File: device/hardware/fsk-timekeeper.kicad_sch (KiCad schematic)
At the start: 19 parts, among them J1 SENSOR, SW1 SW_SPST, U1 SuperMini nRF52840, U2 Ai-Thinker Ra-01SH, U3 TPS61040DBV

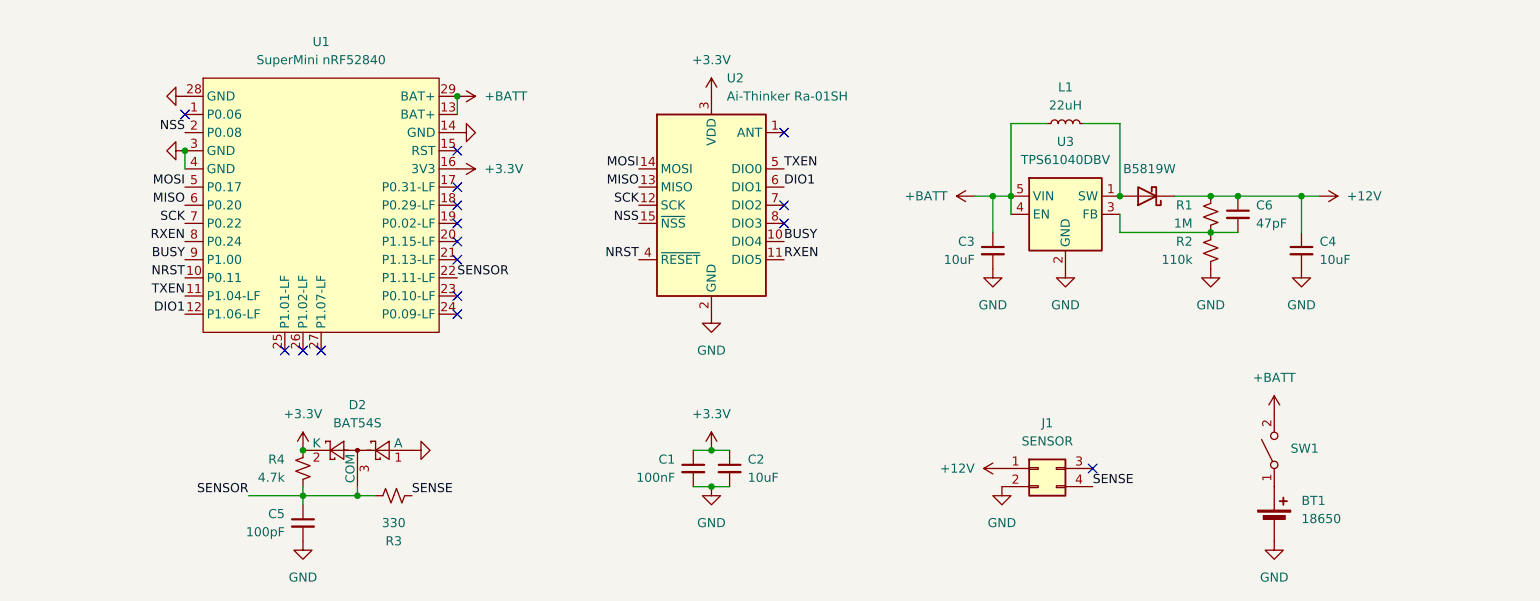
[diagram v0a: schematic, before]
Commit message: add: GPS on the master — ATGM336H, PPS clock calibration, new pin map
Hardware: ATGM336H breakout (U4, master boards only) with a project-local symbol
and footprint; SENSOR moves to P1.13, GPS PPS/RXD/TXD take P0.09/P1.11/P0.10.
Firmware: pin map in config.h; board.c clears UICR.NFCPINS.PROTECT once per
board (readback-guarded reset); the idle SENSOR capture channel captures PPS
on the master; gps.c drives UARTE0 (NMEA, GGA+RMC via $PCAS03), parses fix,
satellites and UTC, and estimates the HFXO error from an 8-64 s window of
gated PPS edges. Reported on the new `P` line (~1 Hz, also in ?STATUS); wire
ticks stay raw, the console applies the correction.

Co-Authored-By: Claude Fable 5.1 <noreply@anthropic.com>
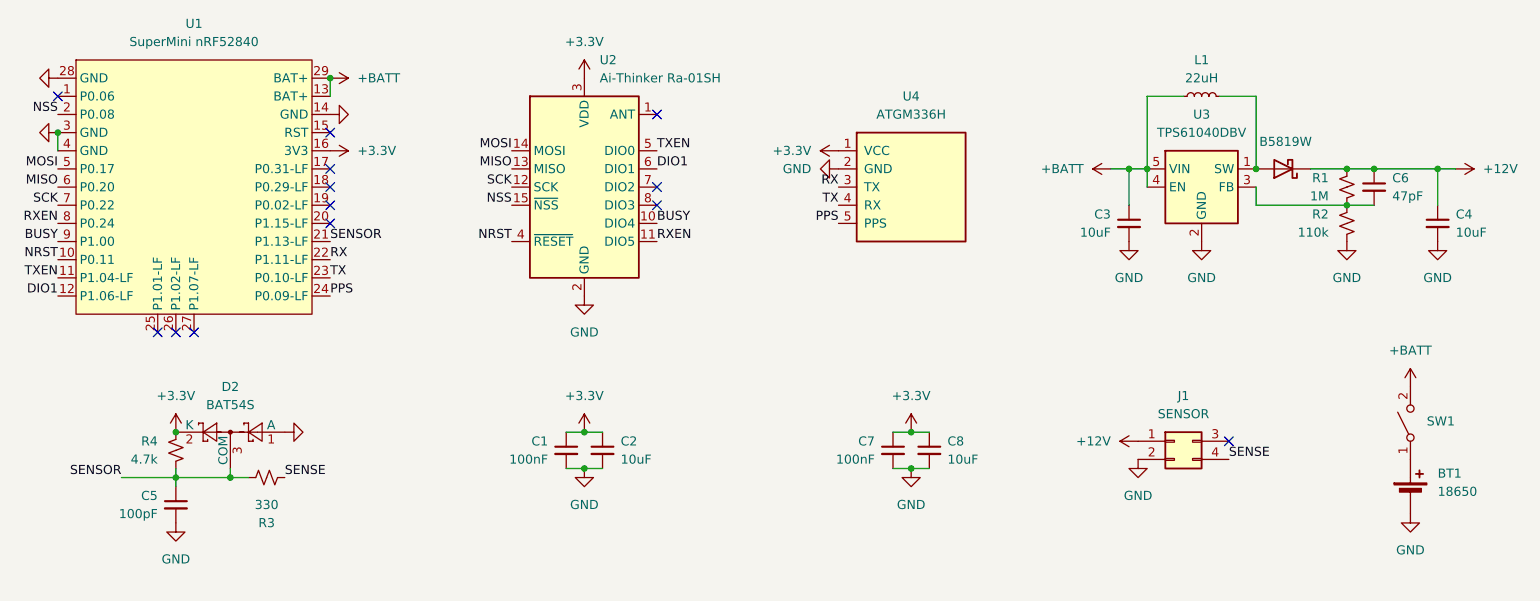
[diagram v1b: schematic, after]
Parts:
- added C7: 100nF, Capacitor_SMD:C_0603_1608Metric, symbol Device:C_Small
- added C8: 10uF, Capacitor_SMD:C_0603_1608Metric, symbol Device:C_Small
- added U4: ATGM336H, lib:ATGM336H_GPS_Module, symbol ATGM336H_GPS_Module:ATGM336H_GPS_Module
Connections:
- net +3.3V: now also C7.1, C8.1, U4.1 (VCC)
- net GND: now also C7.2, C8.2, U4.2 (GND)
- net SENSOR: now also U1.21 (P1.13-LF); no longer U1.22 (P1.11-LF)
- net TX: now reaches U1.23 (P0.10-LF)
- net TX: now also U4.4 (RX)
- net PPS: now reaches U1.24 (P0.09-LF)
- net PPS: now also U4.5 (PPS)
- new net RX: U1.22 (P1.11-LF), U4.3 (TX)
- no-connect marks 16 -> 13
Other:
- moved on the sheet: BT1, C1, C2, C3, C4, C5, C6, D2, J1, L1, R1, R2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

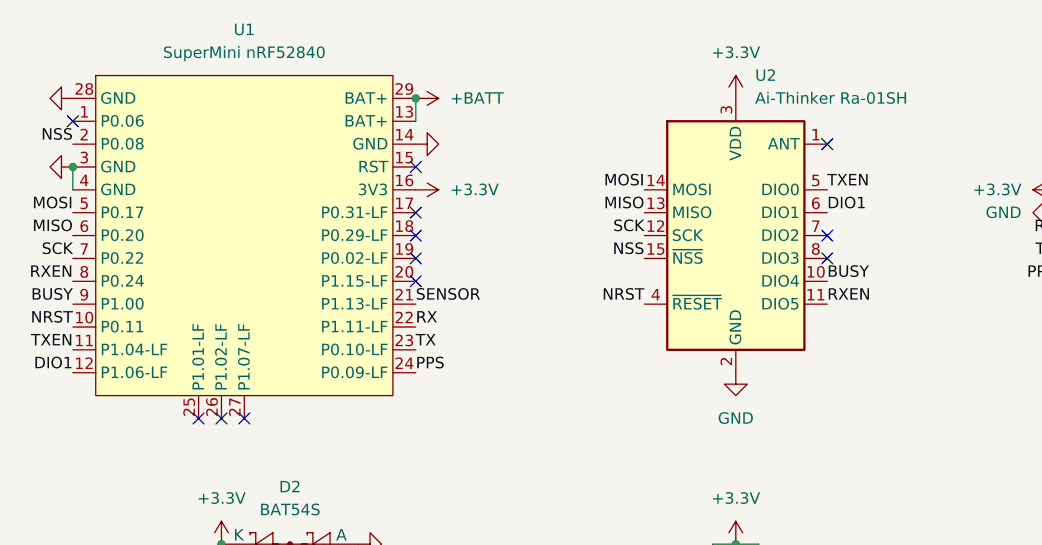
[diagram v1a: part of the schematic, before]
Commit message: fix(hardware): finalize radio wiring, PCB routing and fabrication outputs
Reorganized from:
- 0e2d74b fix: leave the Ra-01SH TXEN and RXEN pins unconnected
- dd02dfc add: stitch the GND pours with vias
- 162bb38 fix: exclude the known ERC items so the check can pass
- 6ef263c fix: remove the track pieces that lie inside pads
- 0b254e7 fix: keep hand-soldered parts out of the JLCPCB BOM and CPL
- 47fa68c add: JLCPCB fabrication files from the assembly plugin

Co-Authored-By: Claude Opus 5.5 <noreply@anthropic.com>
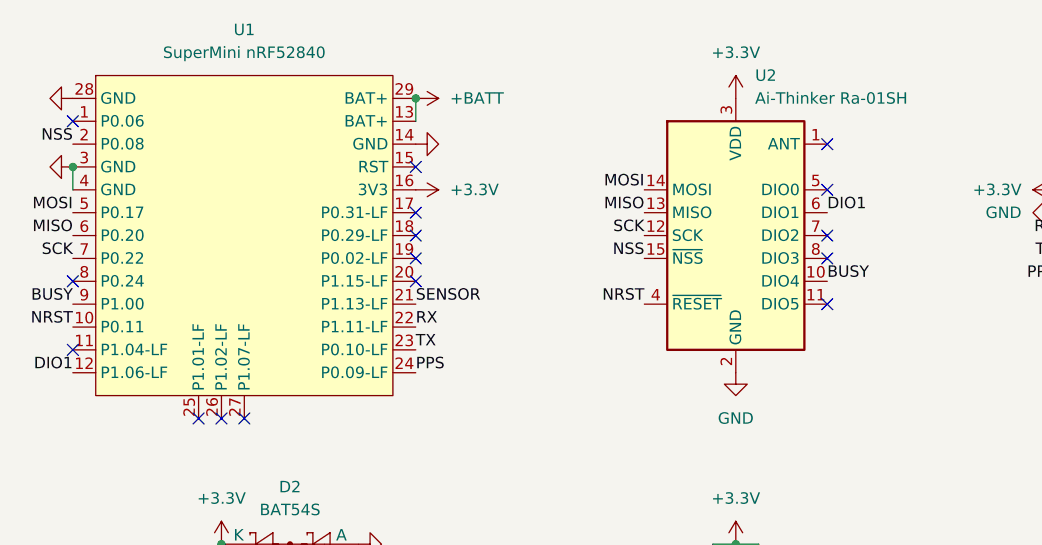
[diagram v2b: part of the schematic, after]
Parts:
- BT1, J1, L1, SW1, U2, U4: now left out of the parts list
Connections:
- net RXEN: no longer names the net of U1.8 (P0.24)
- net RXEN: no longer U2.11 (DIO5)
- net TXEN: no longer names the net of U1.11 (P1.04-LF)
- net TXEN: no longer U2.5 (DIO0)
- no-connect marks 13 -> 17
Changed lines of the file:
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@@
 	)
 	(no_connect
+		(at 48.26 99.06)
+	)
+	(no_connect
 		(at 67.31 106.68)
 	)
 	(no_connect
+		(at 132.08 81.28)
+	)
+	(no_connect
 		(at 86.36 83.82)
 	)
@@
 	)
 	(no_connect
+		(at 48.26 91.44)
+	)
+	(no_connect
 		(at 132.08 76.2)
 	)
@@
 	)
 	(no_connect
+		(at 132.08 93.98)
+	)
+	(no_connect
 		(at 64.77 106.68)
 	)
@@
 		)
 	)
-	(label "TXEN"
-		(at 48.26 99.06 180)
-		(effects
-			(font
-				(size 1.27 1.27)
-			)
-			(justify right bottom)
-		)
-	)
 	(label "SENSE"
 		(at 80.01 127 0)
@@
 		)
 	)
-	(label "RXEN"
-		(at 48.26 91.44 180)
-		(effects
-			(font
-				(size 1.27 1.27)
-			)
-			(justify right bottom)
-		)
-	)
 	(label "SCK"
 		(at 48.26 88.9 180)
@@
 		)
 	)
-	(label "TXEN"
-		(at 132.08 81.28 0)
-		(effects
-			(font
-				(size 1.27 1.27)
-			)
-			(justify left bottom)
-		)
-	)
 	(label "SENSOR"
 		(at 57.15 127 180)
@@
 		)
 	)
-	(label "RXEN"
-		(at 132.08 93.98 0)
-		(effects
-			(font
-				(size 1.27 1.27)
-			)
-			(justify left bottom)
-		)
-	)
 	(label "NSS"
 		(at 111.76 88.9 180)
@@
 		(body_style 1)
 		(exclude_from_sim no)
-		(in_bom yes)
+		(in_bom no)
 		(on_board yes)
-		(in_pos_files yes)
+		(in_pos_files no)
 		(dnp no)
 		(fields_autoplaced yes)
@@
 		(in_bom no)
 		(on_board yes)
-		(in_pos_files yes)
+		(in_pos_files no)
 		(dnp no)
 		(fields_autoplaced yes)
@@
 		(body_style 1)
 		(exclude_from_sim no)
-		(in_bom yes)
+		(in_bom no)
 		(on_board yes)
-		(in_pos_files yes)
+		(in_pos_files no)
 		(dnp no)
 		(fields_autoplaced yes)
@@
 		(body_style 1)
 		(exclude_from_sim no)
-		(in_bom yes)
+		(in_bom no)
 		(on_board yes)
-		(in_pos_files yes)
+		(in_pos_files no)
 		(dnp no)
 		(fields_autoplaced yes)
@@
 		(body_style 1)
 		(exclude_from_sim no)
-		(in_bom yes)
+		(in_bom no)
 		(on_board yes)
-		(in_pos_files yes)
+		(in_pos_files no)
 		(dnp no)
 		(property "Reference" "U4"
@@
 		(body_style 1)
 		(exclude_from_sim no)
-		(in_bom yes)
+		(in_bom no)
 		(on_board yes)
-		(in_pos_files yes)
+		(in_pos_files no)
 		(dnp no)
 		(fields_autoplaced yes)
@@
 		(body_style 1)
 		(exclude_from_sim no)
-		(in_bom yes)
+		(in_bom no)
 		(on_board yes)
-		(in_pos_files yes)
+		(in_pos_files no)
 		(dnp no)
 		(property "Reference" "SW1"

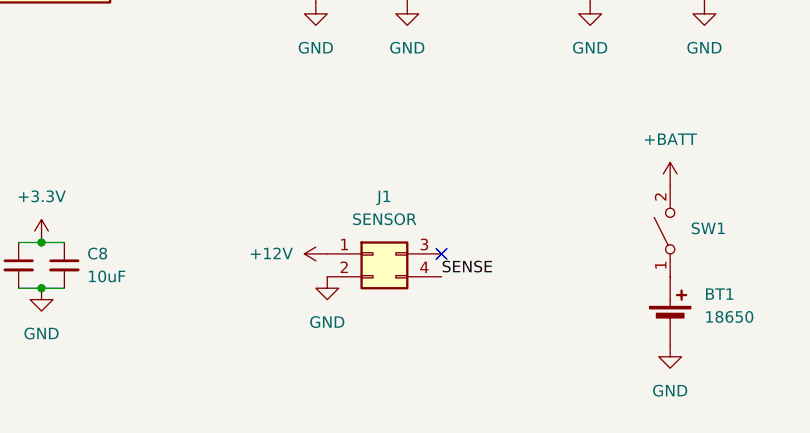
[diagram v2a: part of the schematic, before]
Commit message: fix(hardware): match field-board J1 pinout and revise boost layout
Reorganized from:
- be4e238 fix: match J1 to the field board pinout and tighten the boost layout

Co-Authored-By: Claude Opus 5.5 <noreply@anthropic.com>
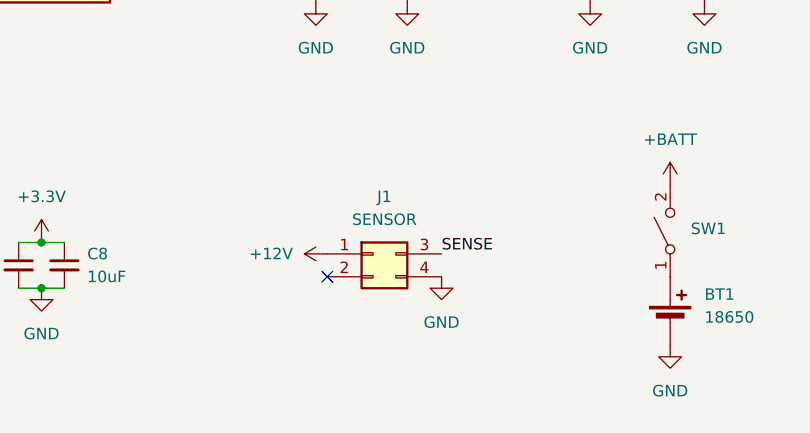
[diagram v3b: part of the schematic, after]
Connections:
- net GND: now also J1.4 (Pin_4); no longer J1.2 (Pin_2)
- net SENSE: now also J1.3 (Pin_3); no longer J1.4 (Pin_4)
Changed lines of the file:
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@@
-	)
-	(no_connect
-		(at 212.09 121.92)
 	)
 	(no_connect
@@
 	(no_connect
 		(at 132.08 93.98)
+	)
+	(no_connect
+		(at 199.39 124.46)
 	)
 	(no_connect
@@
 		)
 	)
-	(label "SENSE"
-		(at 212.09 124.46 0)
-		(effects
-			(font
-				(size 1.27 1.27)
-			)
-			(justify left bottom)
-		)
-	)
 	(label "SENSOR"
 		(at 86.36 93.98 0)
@@
 	(label "DIO1"
 		(at 132.08 83.82 0)
+		(effects
+			(font
+				(size 1.27 1.27)
+			)
+			(justify left bottom)
+		)
+	)
+	(label "SENSE"
+		(at 212.09 121.92 0)
 		(effects
 			(font
@@
 	(symbol
 		(lib_id "power:GND")
-		(at 199.39 124.46 0)
-		(unit 1)
-		(body_style 1)
-		(exclude_from_sim no)
-		(in_bom yes)
-		(on_board yes)
-		(in_pos_files yes)
-		(dnp no)
-		(fields_autoplaced yes)
-		(property "Reference" "#PWR019"
-			(at 199.39 130.81 0)
-			(hide yes)
-			(show_name no)
-			(do_not_autoplace no)
-			(effects
-				(font
-					(size 1.27 1.27)
-				)
-			)
-		)
-		(property "Value" "GND"
-			(at 199.39 129.54 0)
-			(show_name no)
-			(do_not_autoplace no)
-			(effects
-				(font
-					(size 1.27 1.27)
-				)
-			)
-		)
-		(property "Footprint" ""
-			(at 199.39 124.46 0)
-			(hide yes)
-			(show_name no)
-			(do_not_autoplace no)
-			(effects
-				(font
-					(size 1.27 1.27)
-				)
-			)
-		)
-		(property "Datasheet" ""
-			(at 199.39 124.46 0)
-			(hide yes)
-			(show_name no)
-			(do_not_autoplace no)
-			(effects
-				(font
-					(size 1.27 1.27)
-				)
-			)
-		)
-		(property "Description" "Power symbol creates a global label with name \"GND\" , ground"
-			(at 199.39 124.46 0)
-			(hide yes)
-			(show_name no)
-			(do_not_autoplace no)
-			(effects
-				(font
-					(size 1.27 1.27)
-				)
-			)
-		)
-		(pin "1"
-		)
-		(instances
-			(project "fsk-timekeeper"
-				(path "/b99e92f0-86c3-482a-a7ae-e3f31060cbed"
-					(reference "#PWR019")
-					(unit 1)
-				)
-			)
-		)
-	)
-	(symbol
-		(lib_id "power:GND")
 		(at 86.36 76.2 90)
 		(unit 1)
@@
 					(unit 1)
 				)
+			)
+		)
+	)
+	(symbol
+		(lib_id "power:GND")
+		(at 212.09 124.46 0)
+		(unit 1)
+		(body_style 1)
+		(exclude_from_sim no)
+		(in_bom yes)
+		(on_board yes)
+		(in_pos_files yes)
+		(dnp no)
+		(fields_autoplaced yes)
+		(property "Reference" "#PWR019"
+			(at 212.09 130.81 0)
+			(hide yes)
+			(show_name no)
+			(do_not_autoplace no)
+			(effects
+				(font
+					(size 1.27 1.27)
+				)
+			)
+		)
+		(property "Value" "GND"
+			(at 212.09 129.54 0)
+			(show_name no)
+			(do_not_autoplace no)
+			(effects
+				(font
+					(size 1.27 1.27)
+				)
+			)
+		)
+		(property "Footprint" ""
+			(at 212.09 124.46 0)
+			(hide yes)
+			(show_name no)
+			(do_not_autoplace no)
+			(effects
+				(font
+					(size 1.27 1.27)
+				)
+			)
+		)
+		(property "Datasheet" ""
+			(at 212.09 124.46 0)
+			(hide yes)
+			(show_name no)
+			(do_not_autoplace no)
+			(effects
+				(font
+					(size 1.27 1.27)
+				)
+			)
+		)
+		(property "Description" "Power symbol creates a global label with name \"GND\" , ground"
+			(at 212.09 124.46 0)
+			(hide yes)
+			(show_name no)
+			(do_not_autoplace no)
+			(effects
+				(font
+					(size 1.27 1.27)
+				)
+			)
+		)
+		(pin "1"
+		)
+		(instances
+			(project "fsk-timekeeper"
+				(path "/b99e92f0-86c3-482a-a7ae-e3f31060cbed"
+					(reference "#PWR019")
+					(unit 1)
+				)
